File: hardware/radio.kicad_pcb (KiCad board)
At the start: 4 copper layers, 65 x 56 mm, 90 parts, among them J1 JCLK, U1 G144A12, U3V3t1V8 NCP1117ST18T3G, U5V0t3V3 NCP1117ST33T3G

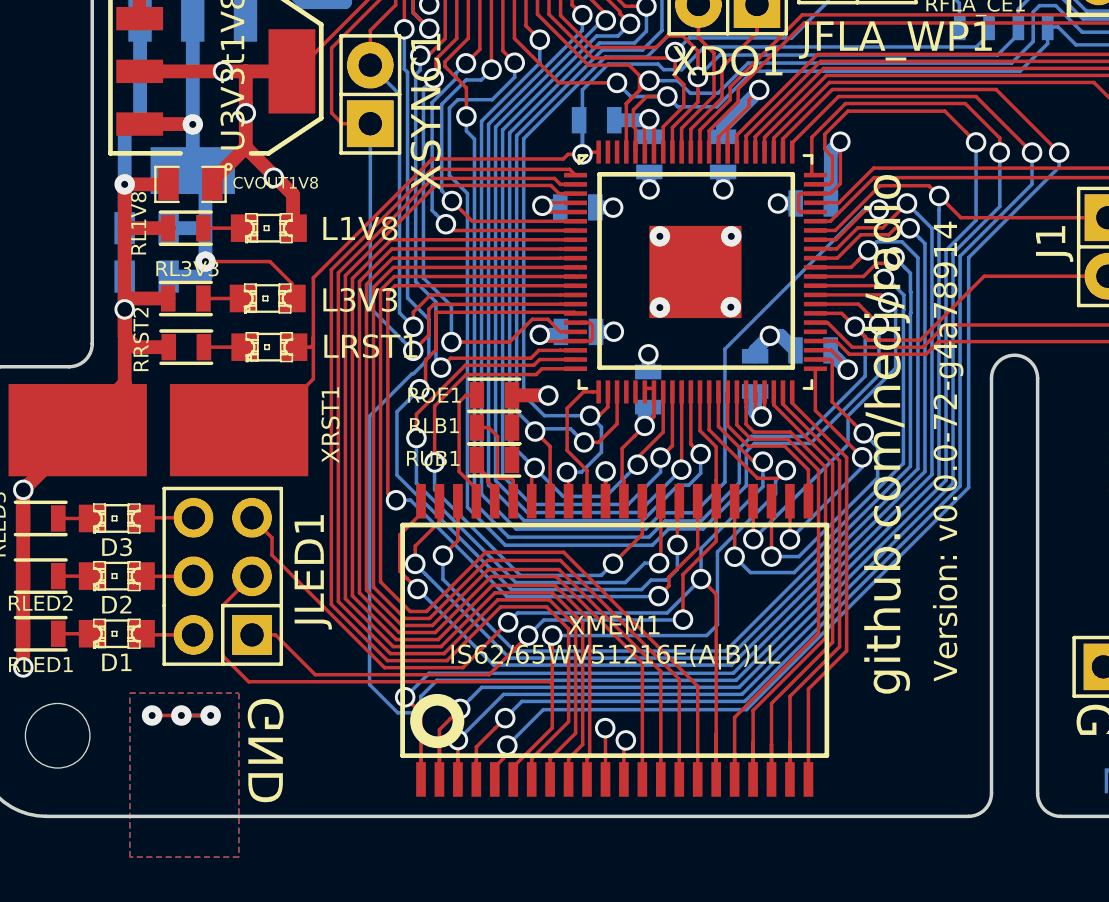
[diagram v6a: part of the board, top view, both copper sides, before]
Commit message: Fixing ground pad.
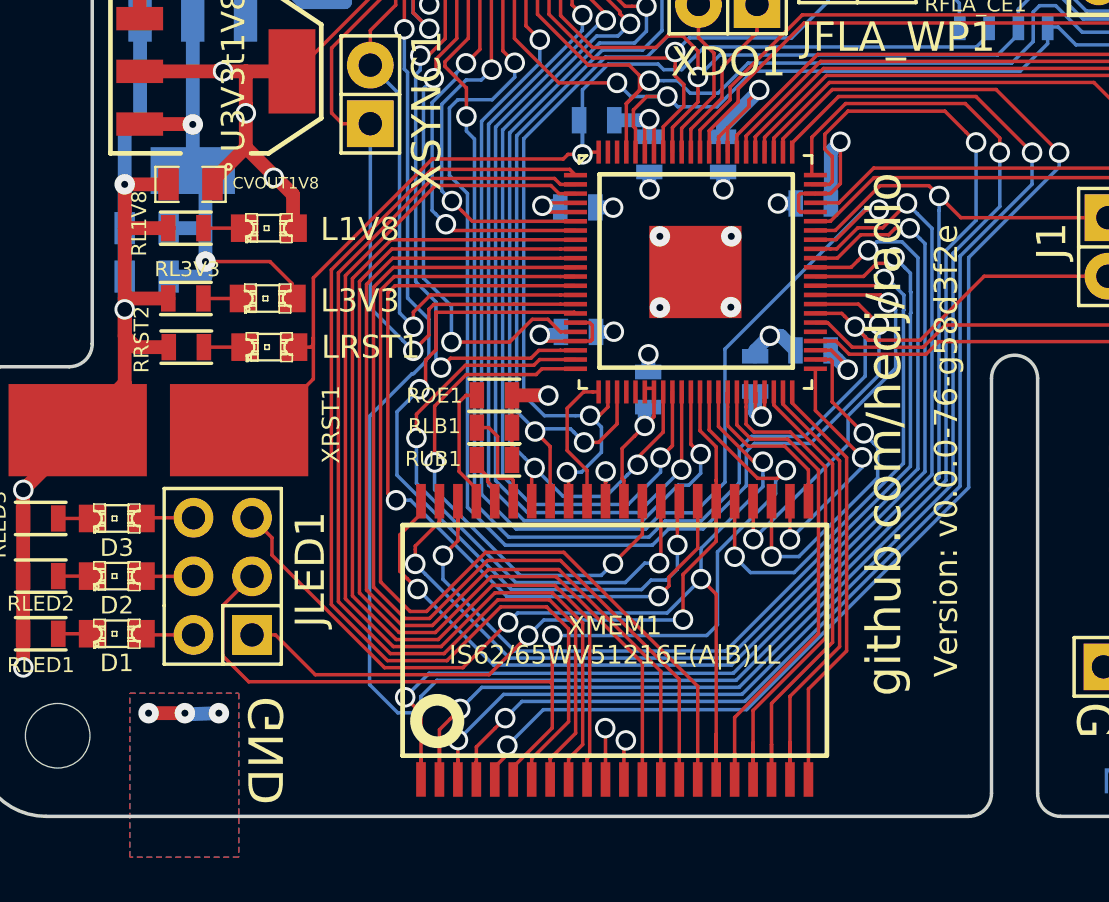
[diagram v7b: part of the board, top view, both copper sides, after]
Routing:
- net GND: track 311.2 -> 316.2 mm, vias 20 -> 23
- net (no net): track 3.81 -> 0.00 mm, vias 3 -> 0
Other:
- board text added: "Version: v0.0.0-76-g58d3f2e"
- board text removed: "Version: v0.0.0-72-g4a78914"
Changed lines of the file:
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@@
     (thickness 1.6)
     (drawings 178)
-    (tracks 1845)
+    (tracks 1848)
     (zones 0)
     (modules 90)
@@
     (effects (font (size 1.5 1.5) (thickness 0.3)) (justify mirror))
   )
-  (gr_text "Version: v0.0.0-72-g4a78914" (at 58.9788 57.4548 90) (layer F.SilkS)
+  (gr_text "Version: v0.0.0-76-g58d3f2e" (at 58.9788 57.4548 90) (layer F.SilkS)
     (effects (font (size 1 1) (thickness 0.1875)))
   )
@@
   (gr_line (start 60.94 54.31) (end 60.94 72.31) (layer Edge.Cuts) (width 0.15))
   (gr_line (start 62.94 54.31) (end 62.94 72.31) (layer Edge.Cuts) (width 0.15))
-  (segment (start 27.0764 68.9356) (end 25.8064 68.9356) (width 0.1524) (layer Bottom) (net 0))
-  (via (at 27.0764 68.9356) (size 0.889) (layers Top Bottom) (net 0))
-  (segment (start 24.5364 68.9356) (end 27.0764 68.9356) (width 0.1524) (layer Top) (net 0))
-  (via (at 24.5364 68.9356) (size 0.889) (layers Top Bottom) (net 0))
-  (via (at 25.8064 68.9356) (size 0.889) (layers Top Bottom) (net 0))
+  (via (at 27.432 68.834) (size 0.889) (layers Top Bottom) (net 1))
+  (segment (start 26.0096 68.8848) (end 27.432 68.834) (width 0.6) (layer Bottom) (net 1))
+  (segment (start 25.9588 68.834) (end 26.0096 68.8848) (width 0.6) (layer Bottom) (net 1))
+  (via (at 25.9588 68.834) (size 0.889) (layers Top Bottom) (net 1))
+  (segment (start 24.384 68.834) (end 25.9588 68.834) (width 0.6) (layer Top) (net 1))
+  (via (at 24.384 68.834) (size 0.889) (layers Top Bottom) (net 1))
+  (segment (start 24.384 66.85) (end 24.384 68.834) (width 0.6) (layer In1.Cu) (net 1))
+  (segment (start 24.384 66.85) (end 42.544856 66.85) (width 0.1524) (layer In1.Cu) (net 1))
   (segment (start 23.3475 51.321955) (end 23.3475 54.5225) (width 0.6) (layer Top) (net 1))
   (segment (start 23.3475 54.5225) (end 21.31 56.56) (width 0.6) (layer Top) (net 1))
@@
   (segment (start 42.544856 66.85) (end 45.081993 69.387137) (width 0.1524) (layer In1.Cu) (net 1))
   (via (at 45.081993 70.015754) (size 0.889) (drill 0.635) (layers Top Bottom) (net 1))
-  (segment (start 18.95 66.85) (end 42.544856 66.85) (width 0.1524) (layer In1.Cu) (net 1))
+  (segment (start 18.95 66.85) (end 24.384 66.85) (width 0.1524) (layer In1.Cu) (net 1))
   (segment (start 45.081993 69.387137) (end 45.081993 70.015754) (width 0.1524) (layer In1.Cu) (net 1))
   (segment (start 44.99878 71.71004) (end 44.99878 70.098967) (width 0.1524) (layer Top) (net 1))
@@
     (min_thickness 0.254)
     (keepout (tracks allowed) (vias allowed) (copperpour not_allowed))
-    (fill (arc_segments 16) (thermal_gap 0.508) (thermal_bridge_width 0.508))
+    (fill yes (arc_segments 16) (thermal_gap 0.508) (thermal_bridge_width 0.508))
     (polygon
       (pts
@@
     (polygon
       (pts
-        (xy 28.2956 75.0824) (xy 23.5712 75.0824) (xy 23.5712 67.9704) (xy 28.2956 67.9704)
+        (xy 28.2956 75.0824) (xy 23.5712 75.0824) (xy 23.5712 67.9704) (xy 28.2956 67.9704) (xy 28.2956 75.0824)
       )
     )
@@
       )
     )
+  )
+  (zone (net 0) (net_name "") (layer B.Mask) (hatch edge 0.508)
+    (connect_pads (clearance 0.508))
+    (min_thickness 0.254)
+    (fill yes (arc_segments 16) (thermal_gap 0.508) (thermal_bridge_width 0.508))
+    (polygon
+      (pts
+        (xy 28.2956 73.2536) (xy 23.5712 73.2536) (xy 23.5712 67.9704) (xy 28.2956 67.9704)
+      )
+    )
+  )
+  (zone (net 0) (net_name "") (layer F.Mask) (hatch edge 0.508)
+    (connect_pads (clearance 0.508))
+    (min_thickness 0.254)
+    (fill yes (arc_segments 16) (thermal_gap 0.508) (thermal_bridge_width 0.508))
+    (polygon
+      (pts
+        (xy 28.2956 73.2536) (xy 23.5712 73.2536) (xy 23.5712 67.9704) (xy 28.2956 67.9704)
+      )
+    )

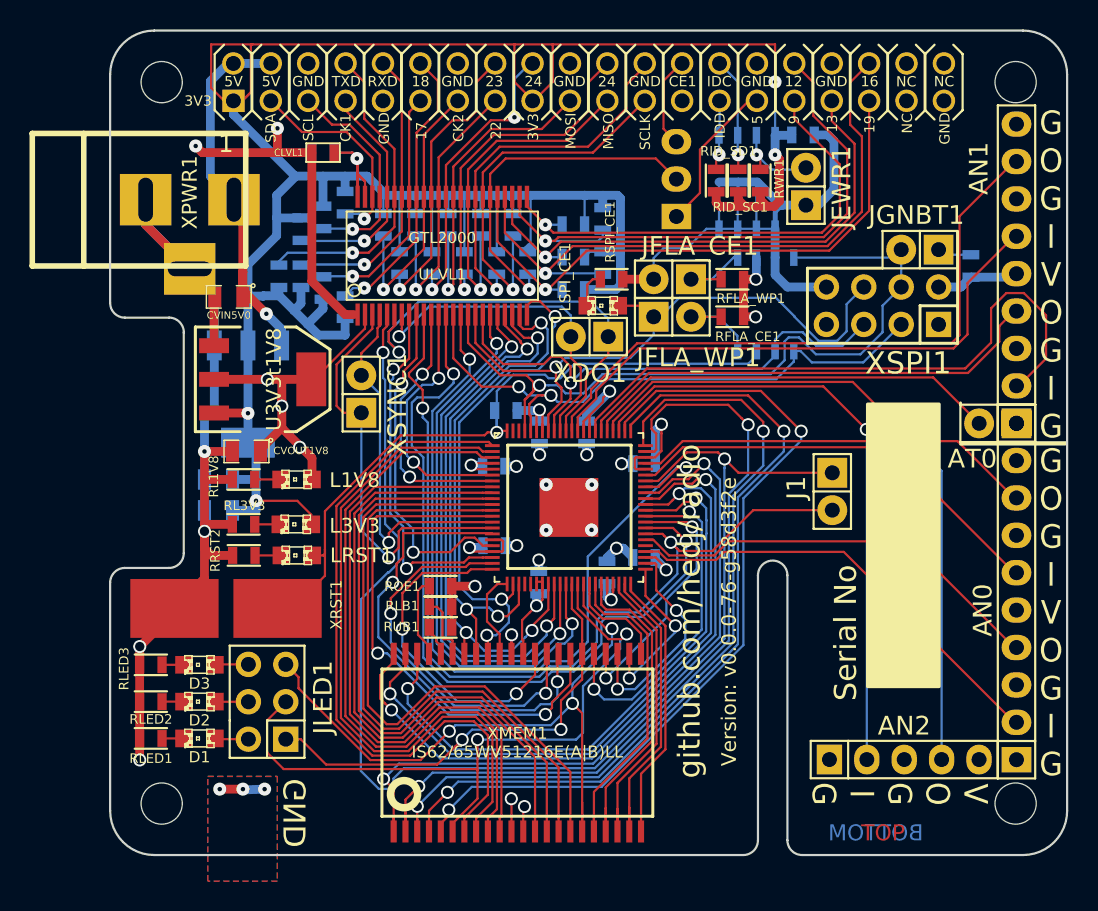
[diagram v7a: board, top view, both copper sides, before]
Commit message: Fix drill size for vias.
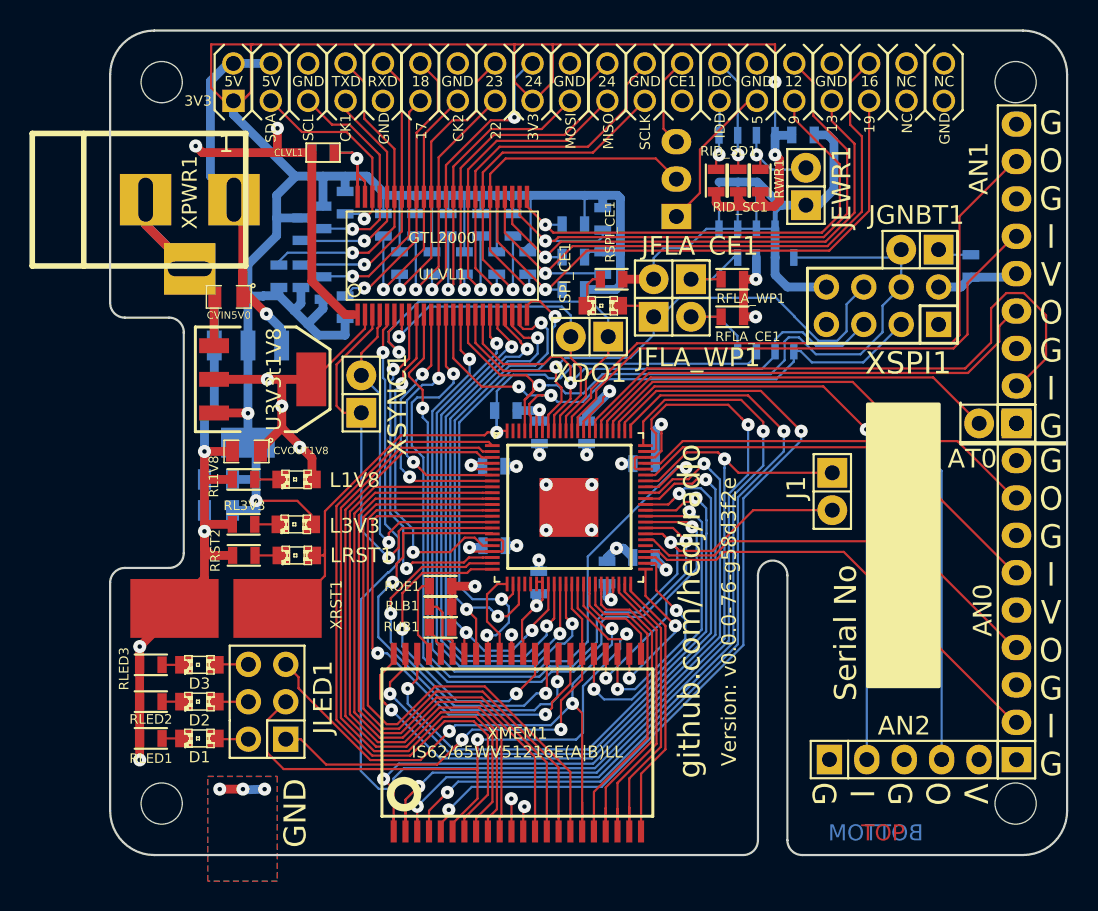
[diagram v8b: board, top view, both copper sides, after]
